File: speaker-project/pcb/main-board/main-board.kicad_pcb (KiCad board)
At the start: 2 copper layers, 100 x 80 mm, 173 parts, among them J1 XT30U-M, J10 UART0, J11 USB-C, J12 JTAG, J13 BT-Modul, J14 Button-PCB, J2 JST-XH-5, J3 JST-XH-5, J4 CHG-STAT, J5 ICP5/USBi, J6 AuxIn 3.5mm, J7 FR-L, J8 FR-R, J9 SUB, Q1 AO4407A, Q2 AO4407A, Q3 MMBT3904, Q4 BC807-40, SW1 RESET, SW2 BOOT, U1 LMR33630ADDA, U2 AMS1117-3.3, U3 ADAU1701JSTZ, U4 24LC32A, U6 TPA3118D2DAP, U7 TPA3118D2DAP, U8 ESP32-S3-WROOM-1-N8R2, U9 USBLC6-2SC6, Y1 12.288MHz

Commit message: Main-Board auf 4 Lagen: In1 GND-Plane, Router auf F/In2/B generalisiert
Beweis: 2-Lagen ist bei dieser Dichte (LQFP-48-DSP + ESP32-Modul + 2x
HTSSOP-Amp + alle Stecker auf 100x80) nicht vollstaendig routbar — zwei
unabhaengige Verfahren (Greedy-Multiseed, PathFinder-Verhandlung)
konvergieren bei ~71 offenen Verbindungen. 3 Signallagen bringen das auf 51.

- autoroute.py: N-Lagen-Routing (NLAYERS env), Vorzugsrichtung je Lage
  H/V/H/V, Durchgangs-Vias verbinden alle Lagen (Via-Spalte muss auf
  jeder Signallage frei sein -> kein Kurzschluss durch In2)
- pcbgen.py: BoardBuilder copper_layers-Parameter
- generate.py: 4-Lagen-Stackup, In1 durchgehende GND-Plane, GND-Fuellung
  auch auf In2
- negotiate.py: PathFinder-Verhandlungsrouter (Diagnose-Werkzeug)

Co-Authored-By: Claude Fable 5 <noreply@anthropic.com>
Claude-Session: https://claude.ai/code/session_01L8xsupY9ovG6C5NDPPgqaH
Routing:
- added copper zone on In1.Cu, net GND
- added copper zone on In2.Cu, net GND
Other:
- copper layers 2 -> 4

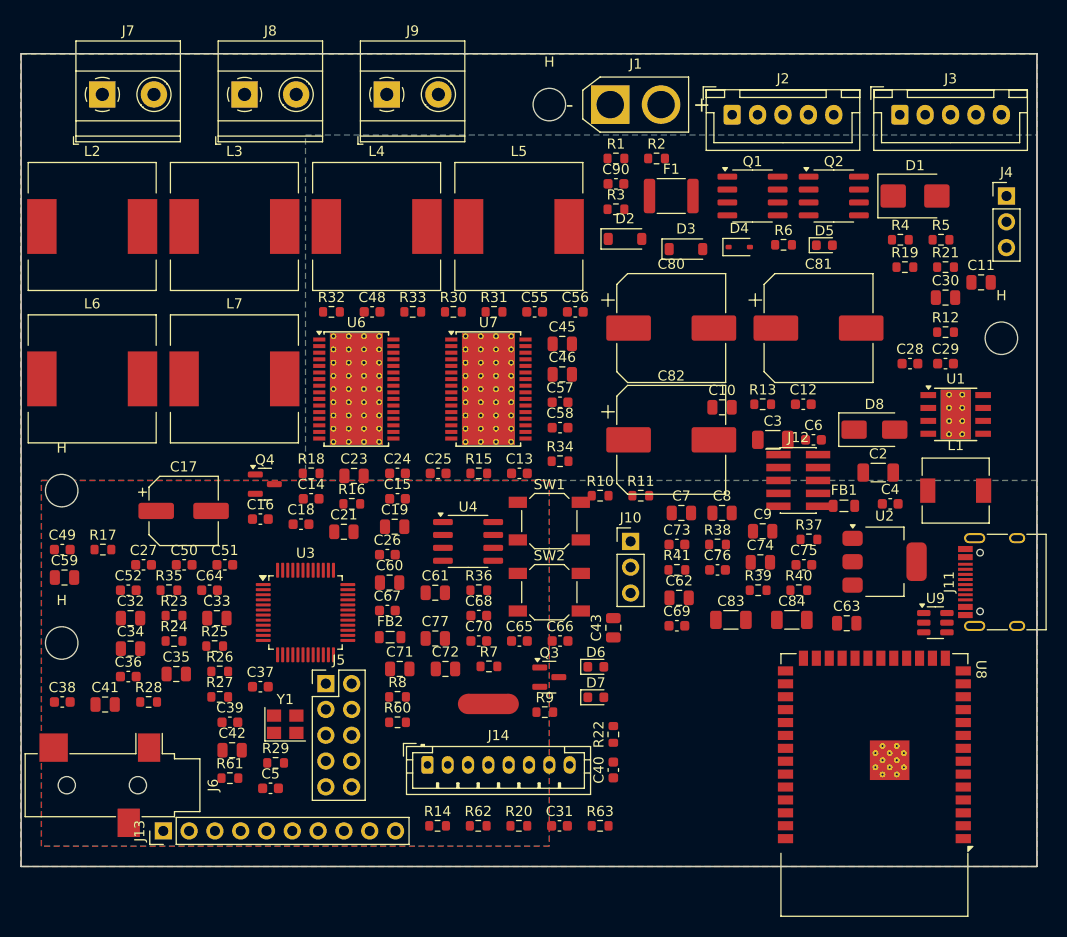
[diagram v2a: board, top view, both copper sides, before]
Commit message: Main-Board ~91% verdrahtet (4-Lagen, ~3080 Bahnen/Vias): GND-Plane+Via-in-Pad, PVDD/AGND/Signale geroutet, 0 thermal/isolated
Ergebnis des Fanout-Routings (0.125mm-Raster, 0.15mm-Bahnen, 0.45mm-Vias,
seed3 + CONNECT_ONLY-Nachlauf): 54 offene Pad-Enden (~38 Netze) + 16 reale
Clearance-Engstellen verbleiben, alle an den Fine-Pitch-Ausbruechen von
ADAU1701 (LQFP-48) und TPA3118 (HTSSOP). Diese Push-and-Shove-Escapes
zwischen 0.5mm-Pins in KiCad interaktiv nachziehen (1-3h) -> fertigungsreif.

- track_width: Amp-Ausgaenge im TIGHT-Modus 0.4mm (bessere Escapes)
- export_fab: 4-Lagen-Gerber (In1/In2)
- Docs (pcb/README, README, BOM) auf tatsaechlichen Status + Nacharbeit

Button-Board bleibt 100% geroutet, DRC-sauber, sofort bestellbar.

Co-Authored-By: Claude Opus 4.8 <noreply@anthropic.com>
Claude-Session: https://claude.ai/code/session_01L8xsupY9ovG6C5NDPPgqaH
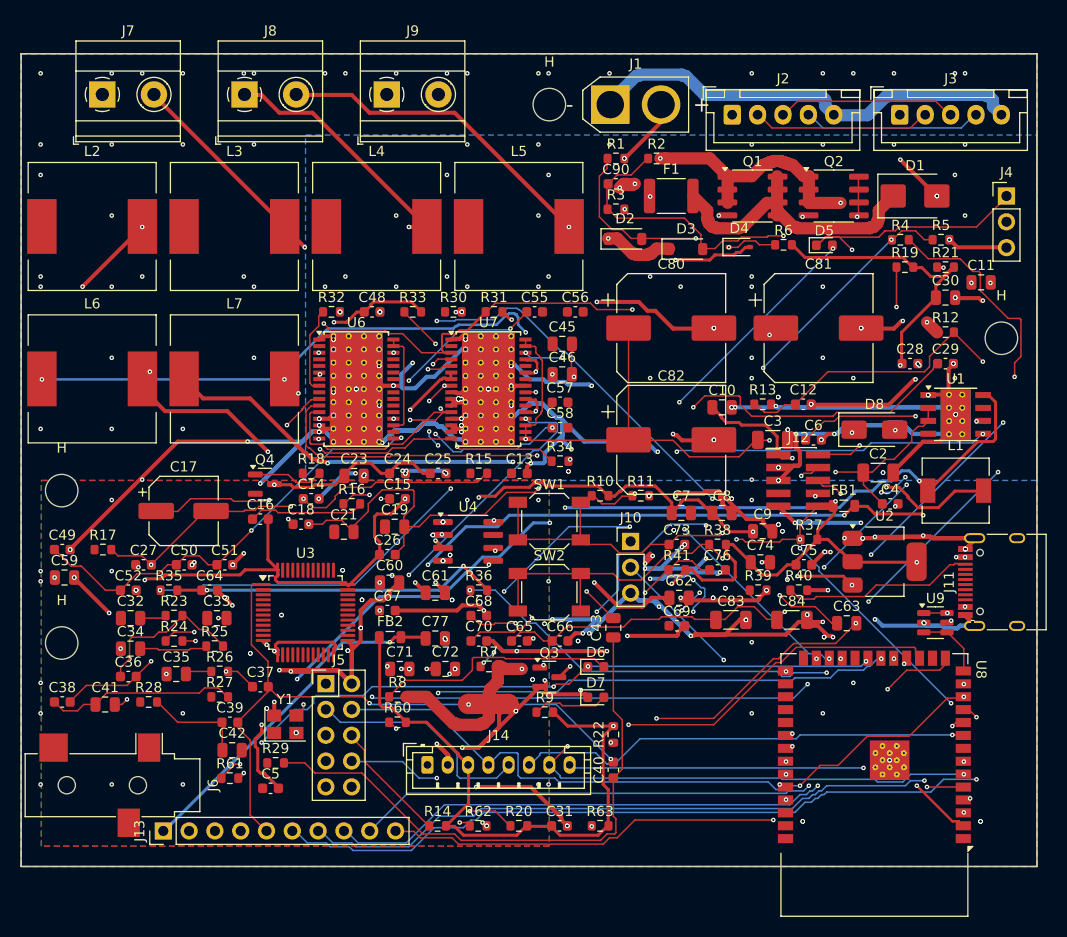
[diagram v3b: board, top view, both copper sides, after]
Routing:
- net GND: track 0.00 -> 1051.6 mm, vias 0 -> 375
- net 3V3: track 0.00 -> 241.4 mm, vias 0 -> 10
- net AGND: track 0.00 -> 230.0 mm, vias 0 -> 14
- net PVDD: track 0.00 -> 221.6 mm, vias 0 -> 8
- net SDA: track 0.00 -> 136.9 mm, vias 0 -> 4
- net 3V3A: track 0.00 -> 126.1 mm, vias 0 -> 7
- net VBAT_P: track 0.00 -> 124.0 mm, vias 0 -> 7
- net CHG_STAT: track 0.00 -> 120.6 mm, vias 0 -> 6
- net FULL_STAT: track 0.00 -> 119.0 mm, vias 0 -> 7
- net SUB_OUT_P: track 0.00 -> 117.7 mm, vias 0 -> 6
- net 5V: track 0.00 -> 104.0 mm, vias 0 -> 6
- net BTN_PWR: track 0.00 -> 103.9 mm, vias 0 -> 5
- net SW5V: track 0.00 -> 99.1 mm, vias 0 -> 5
- net DSP_NRST: track 0.00 -> 96.6 mm, vias 0 -> 6
- net AMP_MUTE: track 0.00 -> 96.5 mm, vias 0 -> 6
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
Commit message: Main-Board via Freerouting verdrahtet: 10 offen (USB-C-Cluster), 0 Shorts (vorher 54)
Freerouting (lokaler Docker-Container) hat 524 Netz-Verbindungen bis auf 10
geroutet — 2800 Bahnen/Vias, 0 Kurzschluesse, 0 isolierte Inseln, 0 starved
thermal. Offen bleibt nur der USB-C-Bereich (VBUS, USB_D+-, CC1/CC2, ADC0_IN,
FB5V) am Platinenrand. Import via eigenem ses_import.py.

Co-Authored-By: Claude Opus 4.8 <noreply@anthropic.com>
Claude-Session: https://claude.ai/code/session_01L8xsupY9ovG6C5NDPPgqaH
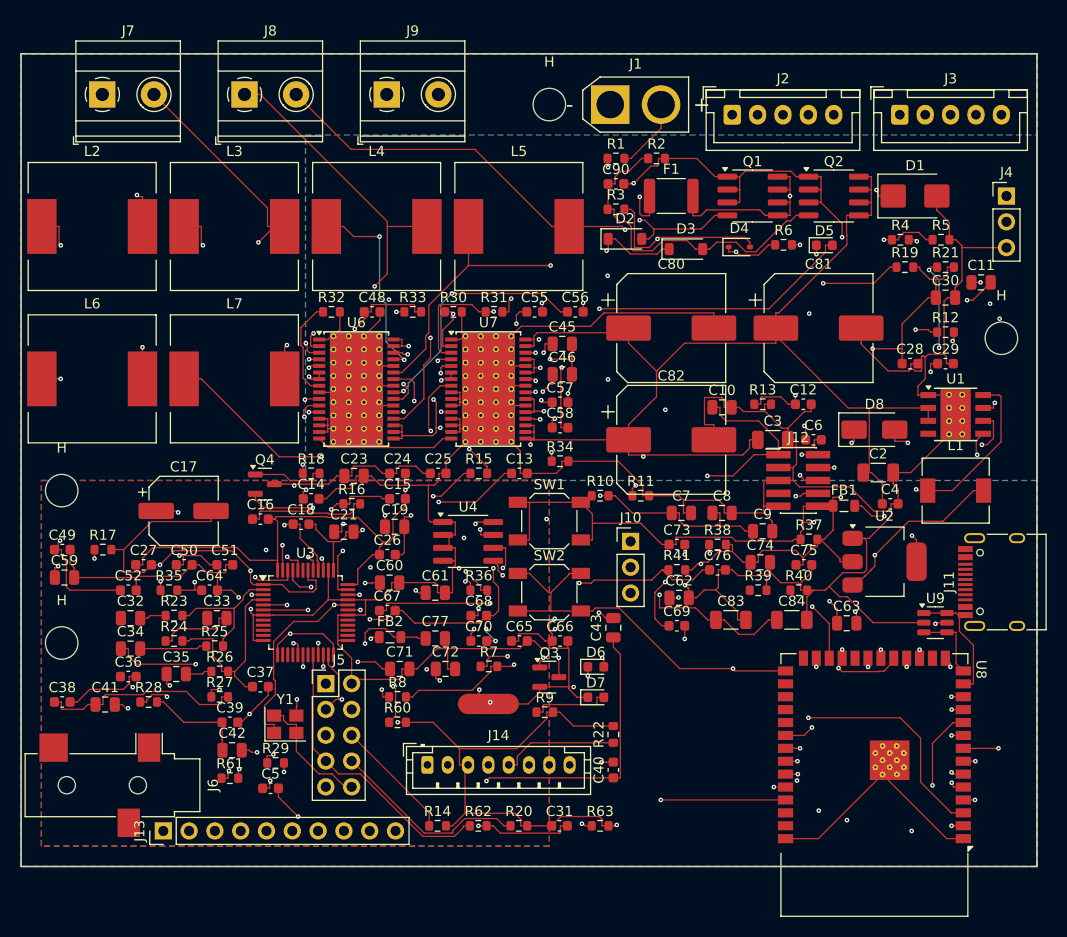
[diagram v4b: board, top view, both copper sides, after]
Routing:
- net GND: track 1051.6 -> 723.2 mm, vias 375 -> 5
- net AMP_SDZ: track 0.00 -> 121.9 mm, vias 0 -> 4
- net U1_BOOT: track 0.00 -> 103.7 mm, vias 0 -> 3
- net 3V3: track 241.4 -> 341.5 mm, vias 10 -> 16
- net U6_OUTPL: track 0.00 -> 79.2 mm, vias 0 -> 3
- net U6_OUTNL: track 0.00 -> 52.9 mm, vias 0 -> 4
- net AGND: track 230.0 -> 281.3 mm, vias 14 -> 13
- net MCLKI: track 0.00 -> 45.4 mm, vias 0 -> 2
- net AMPIN_R: track 0.00 -> 43.8 mm, vias 0 -> 2
- net U6_OUTPR: track 0.00 -> 43.6 mm, vias 0 -> 3
- net PVDD: track 221.6 -> 264.3 mm, vias 8 -> 9
- net EE_WP: track 18.3 -> 59.0 mm
- net U6_OUTNR: track 0.00 -> 40.2 mm, vias 0 -> 2
- net U7_BSNR: track 0.00 -> 37.7 mm, vias 0 -> 3
- net PVDD_PLL: track 74.4 -> 105.5 mm, vias 4 -> 5
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
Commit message: Main-Board ~97% via Freerouting verdrahtet: nur USB-C + 2 GND offen, 0 Shorts
Definitiver Lauf auf bereinigter Platzierung (R10/FB1 entzerrt):
2715 Bahnen/Vias, 10 offene Pad-Enden (5 USB-C-Netze am J11-Rand + 2
GND-Pads), 7 kleine Clearance-Engstellen, 0 Kurzschluesse / 0 isolierte
Inseln / 0 starved-thermal / 0 hole-clearance. Fab (4-Lagen-Gerber) neu.
Docs (pcb/README, README) auf Freerouting-Pipeline + tatsaechlichen Stand.

Co-Authored-By: Claude Opus 4.8 <noreply@anthropic.com>
Claude-Session: https://claude.ai/code/session_01L8xsupY9ovG6C5NDPPgqaH
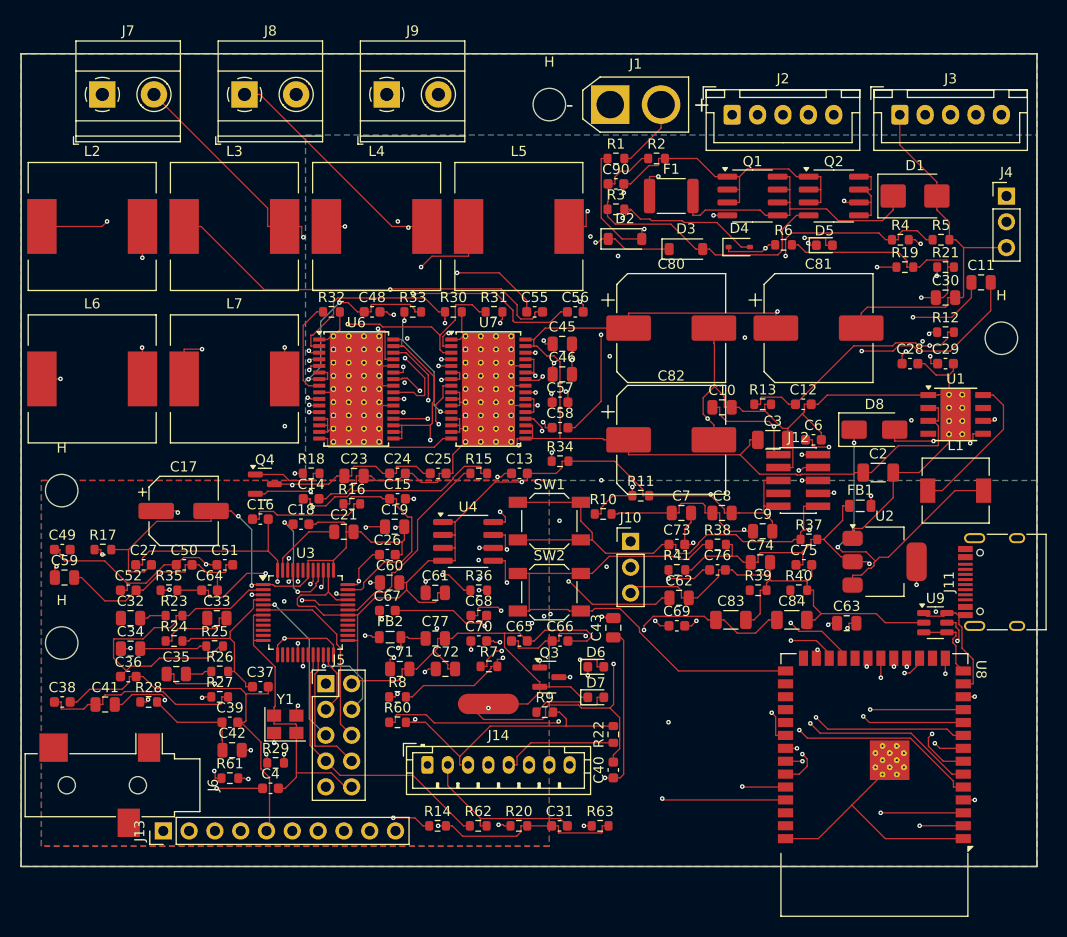
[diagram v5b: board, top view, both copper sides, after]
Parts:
- removed C5: 100n, C_0603_1608Metric
- moved C4 67.1 mm to (24.6, 72.3)
- moved R10 1.82 mm to (57.3, 45.3)
- moved FB1 1.60 mm to (82.6, 44.5)
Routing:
- net U1_BOOT: track 103.7 -> 0.00 mm, vias 3 -> 0
- net SW5V: track 107.4 -> 14.7 mm, vias 3 -> 0
- net ADC0_IN: track 13.4 -> 32.1 mm
- net PVDD: track 264.3 -> 281.2 mm
- net VBAT_P: track 126.4 -> 141.4 mm, vias 5 -> 4
- net BTN_ADC: track 78.2 -> 64.5 mm, vias 2 -> 3
- net SUB_OUT_N: track 77.2 -> 89.1 mm, vias 4 -> 3
- net GND: track 723.2 -> 734.9 mm
- net 5V: track 122.4 -> 111.5 mm, vias 3 -> 4
- net SUB_N: track 83.2 -> 73.3 mm
- net EE_WP: track 59.0 -> 67.8 mm
- net AMP_SDZ: track 121.9 -> 113.0 mm
- net U6_OUTPR: track 43.6 -> 51.5 mm
- net FR_R_N: track 77.2 -> 85.0 mm
- net CHG_STAT: track 118.1 -> 125.9 mm
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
